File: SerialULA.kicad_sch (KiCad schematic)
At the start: 17 parts, among them J1 JTAG-IDC, U1 XC9572XL-10VQG44C, U2 AMS1117-3.3, U3 2C199

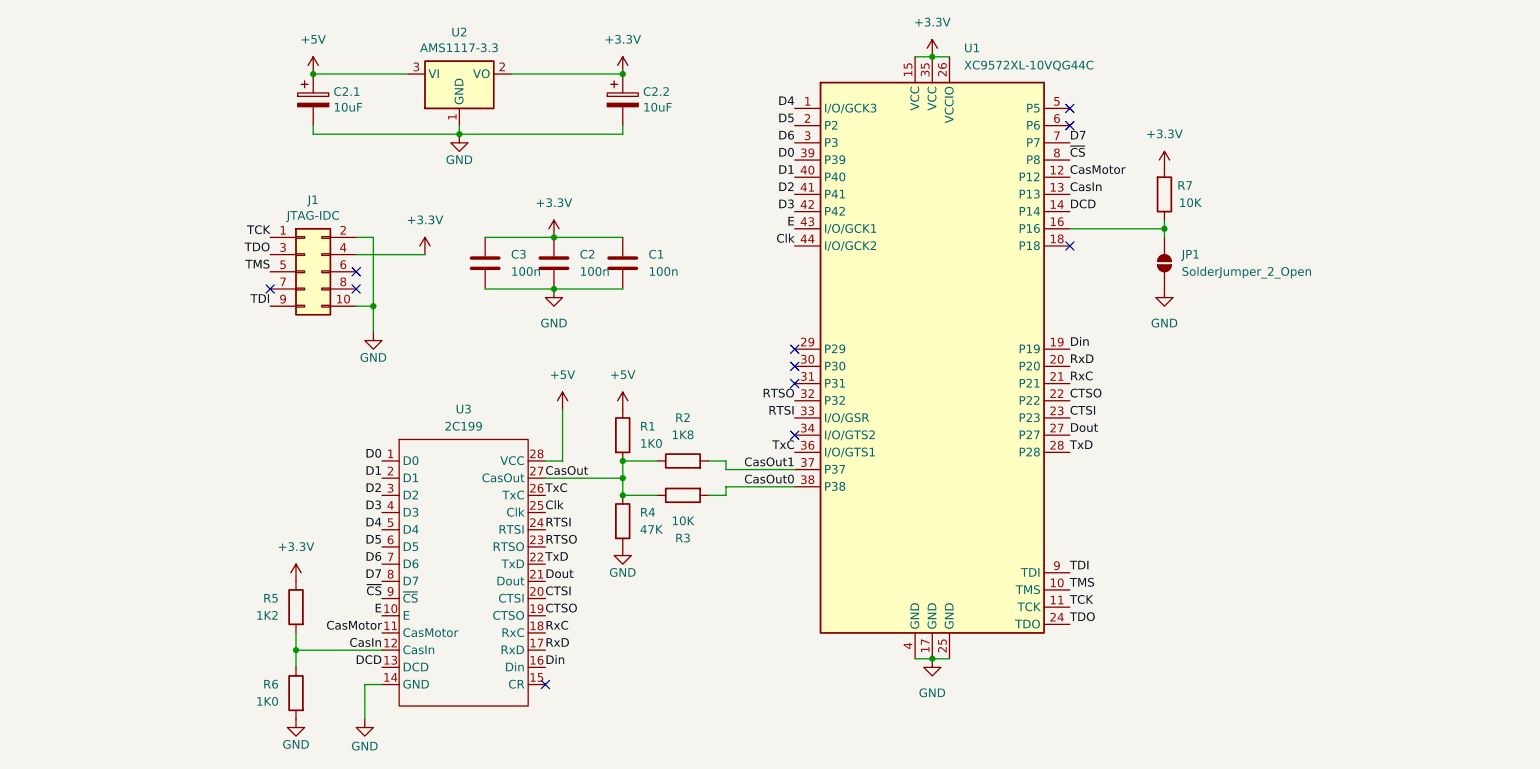
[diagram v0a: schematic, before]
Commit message: Initial commit of Rev 02 hardware
- Dual footprint for both large and small LDO regulator / capacitors.
- Updated resistor values at R1, R2, R3 & R4 for CasOutX. Now pulling up to 3.3V instead of 5V
- Connected extra solder bridge with pull up into spare CPLD input for possible future 'extended features'.
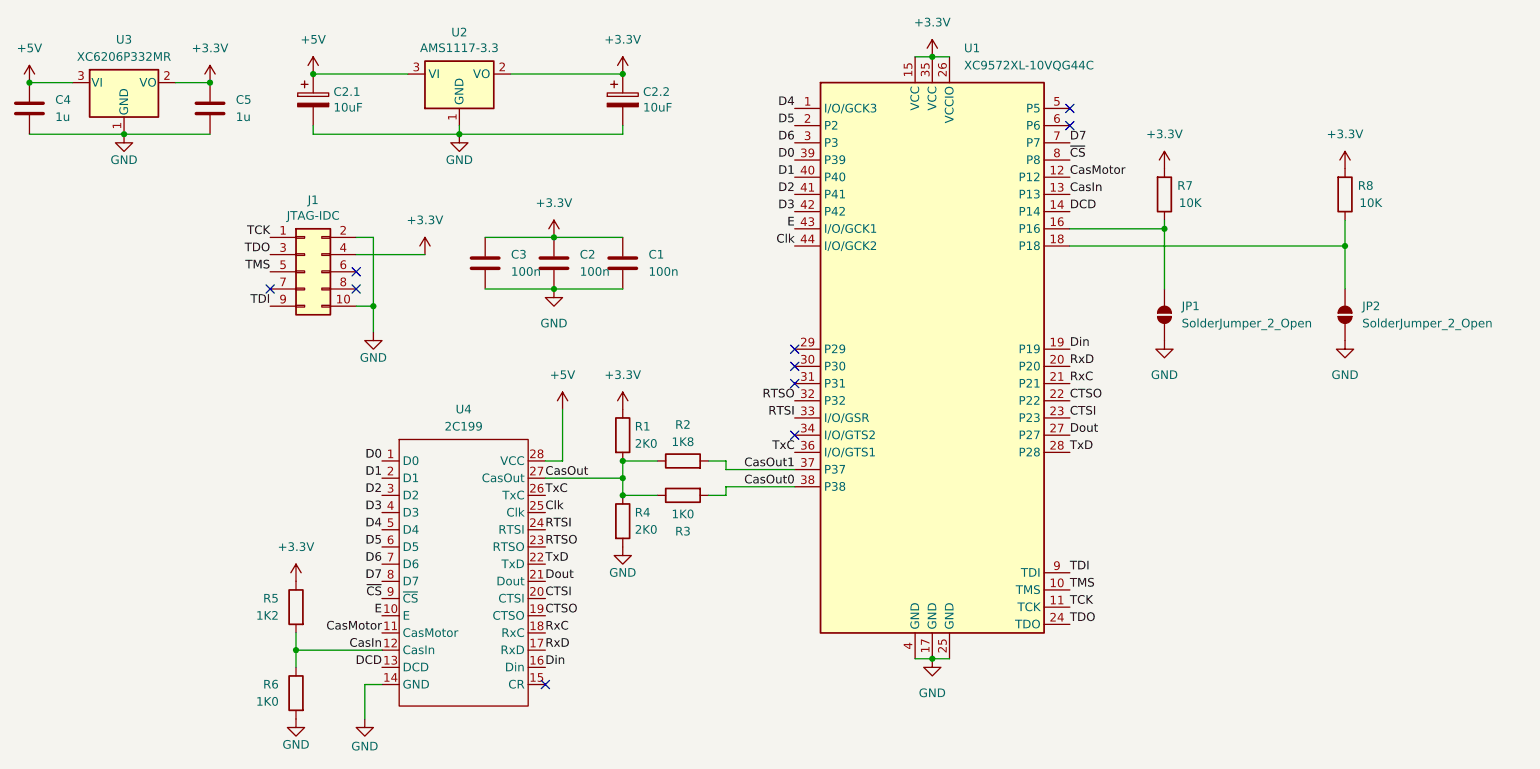
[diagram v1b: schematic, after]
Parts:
- added C4, C5: 1u, Capacitor_SMD:C_0402_1005Metric, symbol Device:C
- added JP2: SolderJumper_2_Open, Jumper:SolderJumper-2_P1.3mm_Open_RoundedPad1.0x1.5mm, symbol Jumper:SolderJumper_2_Open
- added R8: 10K, Resistor_SMD:R_0402_1005Metric, symbol Device:R
- added U3: XC6206P332MR, Package_TO_SOT_SMD:SOT-23-3, symbol Regulator_Linear:XC6206PxxxMR
- C1, C2, C3: LCSC Part # (none) -> C1525
- C2.1, C2.2: LCSC Part # (none) -> C7171
- R1: value 1K0 -> 2K0; JLC Part Number C11702 -> C4109; LCSC Part # (none) -> C4109
- R2: LCSC Part # (none) -> C25871
- R3: value 10K -> 1K0; JLC Part Number C25744 -> C11702; LCSC Part # (none) -> C11702
- R4: value 47K -> 2K0; JLC Part Number C25792 -> C4109; LCSC Part # (none) -> C4109
- R5: LCSC Part # (none) -> C25862
- R6: LCSC Part # (none) -> C11702
- R7: LCSC Part # (none) -> C25744
- U1: LCSC Part # (none) -> C569042
- U2: LCSC Part # (none) -> C6186
- renumbered U3 to U4
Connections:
- net +3.3V: now also R1.1, C5.1, R8.2, U3.2 (VO)
- net +5V: now also C4.1, U3.3 (VI); no longer R1.1
- net GND: now also C4.2, C5.2, JP2.1 (A), U3.1 (GND)
- net at U1.18 (P18): now also JP2.2 (B), R8.1
- no-connect marks 11 -> 10
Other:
- moved on the sheet: JP1
